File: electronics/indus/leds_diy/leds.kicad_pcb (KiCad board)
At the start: 2 copper layers, 230 x 35 mm, 21 parts, among them P1 LED+, P2 THERM, P3 LED-

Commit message: regenerated Gerber Files
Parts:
- moved R1 4.96 mm to (153.6, 77.7), turned to 0 degrees
- turned P2 to 270 degrees
- turned TH1 to 180 degrees
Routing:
- net GND: track 110.4 -> 119.7 mm
- net Net-(P2-Pad2): track 120.1 -> 113.4 mm
- net Net-(P2-Pad3): track 110.0 -> 108.8 mm
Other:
- board text added: "Risebox LEDs v0.1 July 2016"

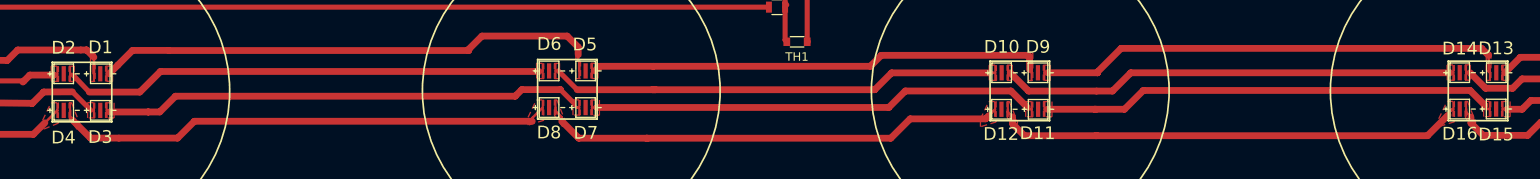
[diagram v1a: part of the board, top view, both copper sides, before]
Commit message: no more DRC errors for LEDS
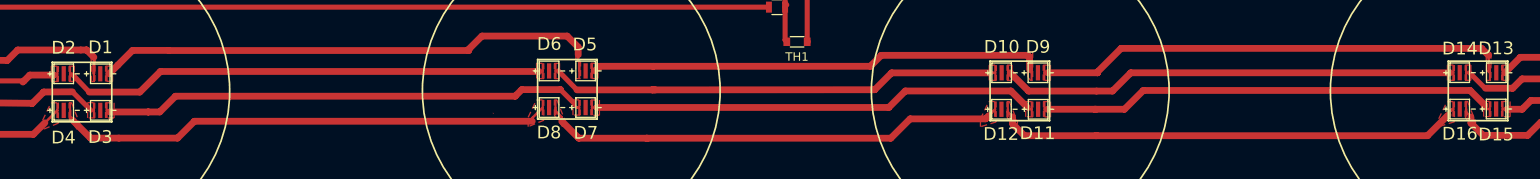
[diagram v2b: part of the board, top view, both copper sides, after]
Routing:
- added copper zone on F.Cu, net Net-(D1-Pad1)
- added copper zone on F.Cu, net Net-(D10-Pad1)
- added copper zone on F.Cu, net Net-(D10-Pad2)
- added copper zone on F.Cu, net Net-(D11-Pad1)
- added copper zone on F.Cu, net Net-(D11-Pad2)
- added copper zone on F.Cu, net Net-(D12-Pad1)
- added copper zone on F.Cu, net Net-(D12-Pad2)
- added copper zone on F.Cu, net Net-(D13-Pad1)
- added copper zone on F.Cu, net Net-(D13-Pad2)
- added copper zone on F.Cu, net Net-(D14-Pad2)
- added copper zone on F.Cu, net Net-(D15-Pad2)
- added copper zone on F.Cu, net Net-(D16-Pad2)
- added copper zone on F.Cu, net Net-(D5-Pad2)

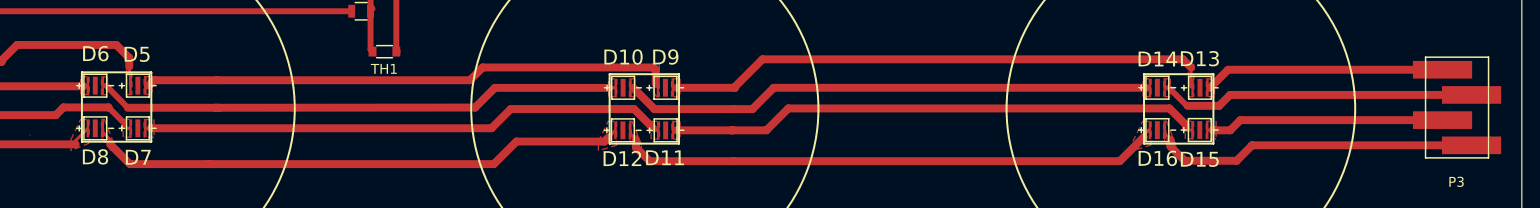
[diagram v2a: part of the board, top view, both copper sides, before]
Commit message: better spacing for LEDs
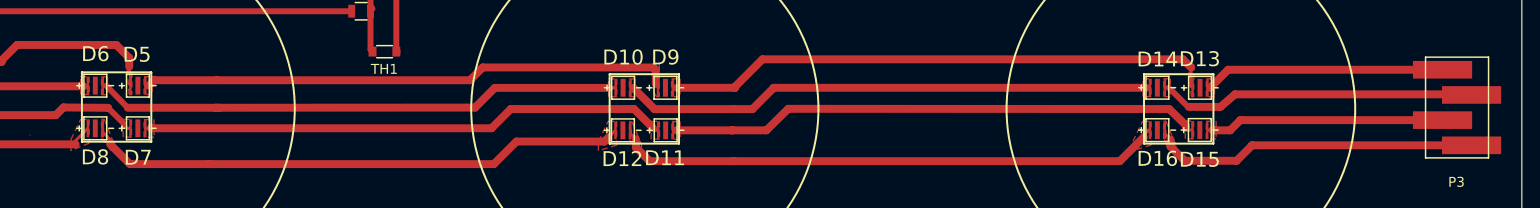
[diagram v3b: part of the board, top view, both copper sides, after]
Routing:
- net Net-(D14-Pad2): track 32.1 -> 32.7 mm
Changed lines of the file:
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@@
   )
   (setup
-    (last_trace_width 0.3)
+    (last_trace_width 0.6)
     (user_trace_width 0.3)
     (user_trace_width 0.8)
@@
   (segment (start 68.9442 85.4897) (end 68.4942 85.6397) (width 0.3) (layer F.Cu) (net 4) (status 10))
   (segment (start 68.4942 85.6397) (end 68.4442 85.6897) (width 0.8) (layer F.Cu) (net 4))
-  (segment (start 123.571 87.3506) (end 128.1176 87.3506) (width 0.8) (layer F.Cu) (net 5))
-  (segment (start 130.0734 89.4588) (end 129.6416 89.154) (width 0.3) (layer F.Cu) (net 5))
-  (segment (start 129.6416 89.154) (end 129.6416 88.8746) (width 0.3) (layer F.Cu) (net 5))
-  (segment (start 129.6416 88.8746) (end 128.1303 87.3633) (width 0.6) (layer F.Cu) (net 5))
+  (segment (start 123.571 87.3506) (end 128.0676 87.3906) (width 0.8) (layer F.Cu) (net 5))
+  (segment (start 130.0734 89.4588) (end 129.5916 89.194) (width 0.3) (layer F.Cu) (net 5))
+  (segment (start 129.5916 89.194) (end 129.5916 88.9146) (width 0.3) (layer F.Cu) (net 5))
+  (segment (start 129.5916 88.9146) (end 128.0803 87.4033) (width 0.6) (layer F.Cu) (net 5))
   (segment (start 79.629 89.9795) (end 80.9879 89.9795) (width 0.8) (layer F.Cu) (net 5))
   (segment (start 122.7963 88.1253) (end 123.571 87.3506) (width 0.8) (layer F.Cu) (net 5))
@@
   (segment (start 80.9879 89.9795) (end 82.8421 88.1253) (width 0.8) (layer F.Cu) (net 5))
   (segment (start 130.0734 89.4588) (end 130.3267 89.4588) (width 0.3) (layer F.Cu) (net 5))
-  (segment (start 128.1176 87.3506) (end 128.1303 87.3633) (width 0.8) (layer F.Cu) (net 5))
+  (segment (start 128.0676 87.3906) (end 128.0803 87.4033) (width 0.8) (layer F.Cu) (net 5))
   (segment (start 74.7442 89.7897) (end 74.8926 89.7897) (width 0.3) (layer F.Cu) (net 5))
   (segment (start 75.0824 89.9795) (end 79.629 89.9795) (width 0.8) (layer F.Cu) (net 5))
@@
   (segment (start 190.96 89.66) (end 194.46 89.66) (width 0.8) (layer F.Cu) (net 15))
   (segment (start 237.02 89.63) (end 237.42 89.63) (width 0.3) (layer F.Cu) (net 15))
-  (segment (start 236.79 89.4) (end 237.02 89.63) (width 0.3) (layer F.Cu) (net 15))
-  (segment (start 236.79 89.13) (end 236.79 89.4) (width 0.8) (layer F.Cu) (net 15))
-  (segment (start 235.11 87.45) (end 236.79 89.13) (width 0.8) (layer F.Cu) (net 15))
-  (segment (start 196.67 87.45) (end 235.11 87.45) (width 0.8) (layer F.Cu) (net 15))
-  (segment (start 194.46 89.66) (end 196.67 87.45) (width 0.8) (layer F.Cu) (net 15))
+  (segment (start 236.77 89.42) (end 237.02 89.63) (width 0.3) (layer F.Cu) (net 15))
+  (segment (start 236.77 89.15) (end 236.77 89.42) (width 0.8) (layer F.Cu) (net 15))
+  (segment (start 235.08 87.51) (end 236.77 89.15) (width 0.8) (layer F.Cu) (net 15))
+  (segment (start 196.66 87.49) (end 235.08 87.51) (width 0.8) (layer F.Cu) (net 15))
+  (segment (start 194.46 89.66) (end 196.66 87.49) (width 0.8) (layer F.Cu) (net 15))
   (segment (start 185.05 89.66) (end 185.38 89.66) (width 0.3) (layer F.Cu) (net 15))
   (segment (start 185.38 89.66) (end 190.96 89.66) (width 0.8) (layer F.Cu) (net 15))
@@
   (segment (start 239.2 85.37) (end 241.02 83.55) (width 0.8) (layer F.Cu) (net 17))
   (segment (start 234.64 85.36) (end 235.04 85.36) (width 0.3) (layer F.Cu) (net 18))
-  (segment (start 236.93 87.19) (end 240.12 87.19) (width 0.8) (layer F.Cu) (net 18))
-  (segment (start 240.12 87.19) (end 241.22 86.09) (width 0.8) (layer F.Cu) (net 18))
-  (segment (start 241.22 86.09) (end 265.575 86.09) (width 0.8) (layer F.Cu) (net 18))
-  (segment (start 236.87 87.19) (end 236.93 87.19) (width 0.3) (layer F.Cu) (net 18))
-  (segment (start 235.04 85.36) (end 236.87 87.19) (width 0.6) (layer F.Cu) (net 18))
+  (segment (start 237.05 87.3) (end 240.24 87.3) (width 0.8) (layer F.Cu) (net 18))
+  (segment (start 240.24 87.3) (end 241.72 86.03) (width 0.8) (layer F.Cu) (net 18))
+  (segment (start 241.72 86.03) (end 266.075 86.03) (width 0.8) (layer F.Cu) (net 18))
+  (segment (start 236.99 87.3) (end 237.05 87.3) (width 0.3) (layer F.Cu) (net 18))
+  (segment (start 235.04 85.36) (end 236.99 87.3) (width 0.6) (layer F.Cu) (net 18))
   (segment (start 262.645 88.63) (end 242.26 88.63) (width 0.8) (layer F.Cu) (net 19))
   (segment (start 239.44 89.63) (end 238.92 89.63) (width 0.3) (layer F.Cu) (net 19))
@@
     (polygon
       (pts
-        (xy 130.4307 86.0595) (xy 129.9307 86.0595) (xy 129.9307 82.8095) (xy 130.4815 82.7968) (xy 130.4815 86.0468)
+        (xy 130.4307 86.0595) (xy 130.2 86.06) (xy 129.9307 82.8095) (xy 130.4815 82.7968) (xy 130.4815 86.0468)
       )
     )
@@
     (polygon
       (pts
-        (xy 235.7747 91.1939) (xy 235.4826 91.8797) (xy 234.5174 90.5335) (xy 234.5174 88.7301) (xy 234.8095 88.7301)
-        (xy 235.7747 91.1939)
+        (xy 234.76 88.74) (xy 235.7747 91.1939) (xy 235.4826 91.8797) (xy 234.5174 90.5335) (xy 234.5174 88.7301)
+        (xy 234.76 88.74)
       )
     )
@@
     (polygon
       (pts
-        (xy 237.5117 86.2725) (xy 237.0117 86.2725) (xy 237.0117 83.0225) (xy 237.5625 83.0098) (xy 237.5625 86.2598)
+        (xy 237.5117 86.2725) (xy 237.32 86.28) (xy 237.0117 83.0225) (xy 237.5625 83.0098) (xy 237.5625 86.2598)
       )
     )
@@
     (polygon
       (pts
-        (xy 181.8919 91.222) (xy 181.5998 91.9078) (xy 180.6346 90.5616) (xy 180.6346 88.7582) (xy 180.9267 88.7582)
-        (xy 181.8919 91.222)
-      )
-    )
+        (xy 180.96 88.89) (xy 181.8919 91.222) (xy 181.5998 91.9078) (xy 180.6346 90.5616) (xy 180.6346 88.7582)
+        (xy 180.96 88.89)
+      )
+    )

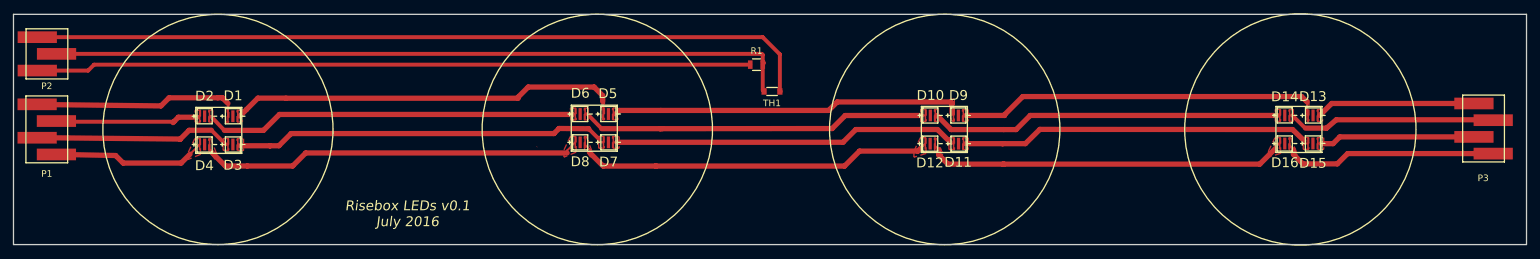
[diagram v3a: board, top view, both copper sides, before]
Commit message: add ground zone on F Cu
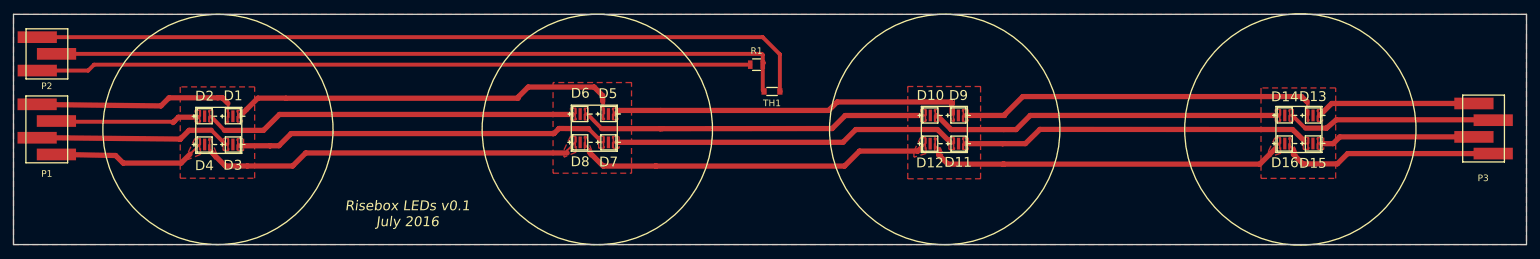
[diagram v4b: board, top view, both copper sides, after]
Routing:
- added copper zone on F.Cu, net GND
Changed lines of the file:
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@@
     (trace_clearance 0.3)
     (zone_clearance 0.508)
-    (zone_45_only no)
+    (zone_45_only yes)
     (trace_min 0.254)
     (segment_width 0.2)
@@
     (polygon
       (pts
-        (xy 120.2018 90.1474) (xy 120.201727 90.133587) (xy 120.2218 90.1274) (xy 120.2018 90.1474)
-      )
-    )
-  )
-  (zone (net 7) (net_name "Net-(D4-Pad2)") (layer F.Cu) (hatch edge 0.508)
-    (connect_pads yes (clearance 0.508))
-    (min_thickness 0.254)
-    (fill yes (arc_segments 16) (thermal_gap 0.508) (thermal_bridge_width 0.508))
-    (polygon
-      (pts
         (xy 126.1753 90.9476) (xy 124.3211 91.7096) (xy 124.3211 90.6047) (xy 125.299 88.56) (xy 126.16 88.56)
         (xy 126.1753 90.9476)
@@
       )
     )
+  )
+  (zone (net 21) (net_name GND) (layer F.Cu) (hatch edge 0.508)
+    (connect_pads yes (clearance 0.508))
+    (min_thickness 0.254)
+    (fill yes (arc_segments 16) (thermal_gap 0.508) (thermal_bridge_width 0.508))
+    (polygon
+      (pts
+        (xy 270.63 105) (xy 40.64 105) (xy 40.64 70.01) (xy 270.63 70.01) (xy 270.63 105)
+      )
+    )
+    (polygon
+      (pts        (xy 176.58 80.97) (xy 176.58 95) (xy 187.65 95) (xy 187.65 80.97) (xy 176.58 80.97)
+      )
+    )
+    (polygon
+      (pts        (xy 230.28 81.19) (xy 230.28 94.94) (xy 241.63 94.94) (xy 241.63 81.19) (xy 230.28 81.19)
+      )
+    )
+    (polygon
+      (pts        (xy 65.99 81.03) (xy 65.99 94.91) (xy 77.3 94.91) (xy 77.3 81.03) (xy 65.99 81.03)
+      )
+    )
+    (polygon
+      (pts        (xy 122.66 80.37) (xy 122.66 94.15) (xy 134.59 94.15) (xy 134.59 80.37) (xy 122.66 80.37)
+      )
+    )
